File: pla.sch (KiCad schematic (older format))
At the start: 16 parts, among them U12 74LS02, U14 74LS139, U15 74LS175, U16 MOS_251641_PLA, U19 ATF16V8

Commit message: Enlarge drill holes to 0.9mm in order to make it possible to use ZIF sockets
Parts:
- U12: footprint Package_DIP:DIP-14_W7.62mm_Socket_LongPads -> LittleSixteen:DIP-14_W7.62mm_Socket_LongPads
- U14, U15: footprint Package_DIP:DIP-16_W7.62mm_Socket_LongPads -> LittleSixteen:DIP-16_W7.62mm_Socket_LongPads
- U16: footprint Package_DIP:DIP-28_W15.24mm_Socket_LongPads -> LittleSixteen:DIP-28_W15.24mm_Socket_LongPads
- U19: footprint Package_DIP:DIP-20_W7.62mm_Socket_LongPads -> LittleSixteen:DIP-20_W7.62mm_Socket_LongPads
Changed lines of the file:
@@
 F 0 "U14" H 9280 5531 50  0000 L CNN
 F 1 "74LS139" H 9280 5440 50  0000 L CNN
-F 2 "Package_DIP:DIP-16_W7.62mm_Socket_LongPads" H 9050 5485 50  0001 C CNN
+F 2 "LittleSixteen:DIP-16_W7.62mm_Socket_LongPads" H 9050 5485 50  0001 C CNN
 F 3 "http://www.ti.com/lit/gpn/sn74LS139" H 9050 5485 50  0001 C CNN
 	3    9050 5485
@@
 F 0 "U12" H 7495 5531 50  0000 L CNN
 F 1 "74LS02" H 7495 5440 50  0000 L CNN
-F 2 "Package_DIP:DIP-14_W7.62mm_Socket_LongPads" H 7265 5485 50  0001 C CNN
+F 2 "LittleSixteen:DIP-14_W7.62mm_Socket_LongPads" H 7265 5485 50  0001 C CNN
 F 3 "http://www.ti.com/lit/gpn/sn74ls02" H 7265 5485 50  0001 C CNN
 	5    7265 5485
@@
 F 0 "U19" H 3840 7075 50  0000 C CNN
 F 1 "ATF16V8" H 3840 6984 50  0000 C CNN
-F 2 "Package_DIP:DIP-20_W7.62mm_Socket_LongPads" H 3840 6260 50  0001 C CNN
+F 2 "LittleSixteen:DIP-20_W7.62mm_Socket_LongPads" H 3840 6260 50  0001 C CNN
 F 3 "DOCUMENTATION" H 3840 6260 50  0001 C CNN
 	1    3840 6260
@@
 F 0 "U16" H 2395 3200 50  0000 C CNN
 F 1 "MOS_251641_PLA" H 2395 3109 50  0000 C CNN
-F 2 "Package_DIP:DIP-28_W15.24mm_Socket_LongPads" H 2395 1985 50  0001 C CNN
+F 2 "LittleSixteen:DIP-28_W15.24mm_Socket_LongPads" H 2395 1985 50  0001 C CNN
 F 3 "DOCUMENTATION" H 2395 1985 50  0001 C CNN
 	1    2395 1985
@@
 F 0 "U16" H 8822 3576 50  0000 R CNN
 F 1 "MOS_251641_PLA" H 8822 3485 50  0000 R CNN
-F 2 "Package_DIP:DIP-28_W15.24mm_Socket_LongPads" H 9050 3530 50  0001 C CNN
+F 2 "LittleSixteen:DIP-28_W15.24mm_Socket_LongPads" H 9050 3530 50  0001 C CNN
 F 3 "DOCUMENTATION" H 9050 3530 50  0001 C CNN
 	2    9050 3530
@@
 F 0 "U12" H 8105 3075 50  0000 C CNN
 F 1 "74LS02" H 8105 2984 50  0000 C CNN
-F 2 "Package_DIP:DIP-14_W7.62mm_Socket_LongPads" H 8105 2750 50  0001 C CNN
+F 2 "LittleSixteen:DIP-14_W7.62mm_Socket_LongPads" H 8105 2750 50  0001 C CNN
 F 3 "http://www.ti.com/lit/gpn/sn74ls02" H 8105 2750 50  0001 C CNN
 	3    8105 2750
@@
 F 0 "U12" H 8105 2375 50  0000 C CNN
 F 1 "74LS02" H 8105 2284 50  0000 C CNN
-F 2 "Package_DIP:DIP-14_W7.62mm_Socket_LongPads" H 8105 2050 50  0001 C CNN
+F 2 "LittleSixteen:DIP-14_W7.62mm_Socket_LongPads" H 8105 2050 50  0001 C CNN
 F 3 "http://www.ti.com/lit/gpn/sn74ls02" H 8105 2050 50  0001 C CNN
 	2    8105 2050
@@
 F 0 "U14" H 9650 2517 50  0000 C CNN
 F 1 "74LS139" H 9650 2426 50  0000 C CNN
-F 2 "Package_DIP:DIP-16_W7.62mm_Socket_LongPads" H 9650 2150 50  0001 C CNN
+F 2 "LittleSixteen:DIP-16_W7.62mm_Socket_LongPads" H 9650 2150 50  0001 C CNN
 F 3 "http://www.ti.com/lit/gpn/sn74LS139" H 9650 2150 50  0001 C CNN
 	2    9650 2150
@@
 F 0 "U14" H 8115 1652 50  0000 C CNN
 F 1 "74LS139" H 8115 1561 50  0000 C CNN
-F 2 "Package_DIP:DIP-16_W7.62mm_Socket_LongPads" H 8115 1285 50  0001 C CNN
+F 2 "LittleSixteen:DIP-16_W7.62mm_Socket_LongPads" H 8115 1285 50  0001 C CNN
 F 3 "http://www.ti.com/lit/gpn/sn74LS139" H 8115 1285 50  0001 C CNN
 	1    8115 1285
@@
 F 0 "U12" H 4660 1668 50  0000 C CNN
 F 1 "74LS02" H 4660 1759 50  0000 C CNN
-F 2 "Package_DIP:DIP-14_W7.62mm_Socket_LongPads" H 4660 1985 50  0001 C CNN
+F 2 "LittleSixteen:DIP-14_W7.62mm_Socket_LongPads" H 4660 1985 50  0001 C CNN
 F 3 "http://www.ti.com/lit/gpn/sn74ls02" H 4660 1985 50  0001 C CNN
 	1    4660 1985
@@
 F 0 "U15" H 6380 2135 50  0000 C CNN
 F 1 "74LS175" H 6435 930 50  0000 C CNN
-F 2 "Package_DIP:DIP-16_W7.62mm_Socket_LongPads" H 6165 1585 50  0001 C CNN
+F 2 "LittleSixteen:DIP-16_W7.62mm_Socket_LongPads" H 6165 1585 50  0001 C CNN
 F 3 "http://www.ti.com/lit/gpn/sn74LS175" H 6165 1585 50  0001 C CNN
 	1    6165 1585

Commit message: Use clearer diode footprint
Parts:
- D80, D81, D82, D83, D84, D85: footprint Diode_THT:D_DO-35_SOD27_P5.08mm_Vertical_KathodeUp -> LittleSixteen:D_DO-35_SOD27_P5.08mm_Vertical_KathodeUp
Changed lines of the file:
@@
 F 0 "D80" H 2335 5455 50  0000 C CNN
 F 1 "1n4148" H 2325 5550 50  0000 C CNN
-F 2 "Diode_THT:D_DO-35_SOD27_P5.08mm_Vertical_KathodeUp" H 2225 5405 50  0001 C CNN
+F 2 "LittleSixteen:D_DO-35_SOD27_P5.08mm_Vertical_KathodeUp" H 2225 5405 50  0001 C CNN
 F 3 "~" H 2225 5405 50  0001 C CNN
 F 4 "Only mount if using PLA16V8" H 2225 5405 50  0001 C CNN "Notes"
@@
 F 0 "D81" H 2140 5265 50  0000 C CNN
 F 1 "1n4148" H 2025 5179 50  0001 C CNN
-F 2 "Diode_THT:D_DO-35_SOD27_P5.08mm_Vertical_KathodeUp" H 2025 5305 50  0001 C CNN
+F 2 "LittleSixteen:D_DO-35_SOD27_P5.08mm_Vertical_KathodeUp" H 2025 5305 50  0001 C CNN
 F 3 "~" H 2025 5305 50  0001 C CNN
 F 4 "Only mount if using PLA16V8" H 2025 5305 50  0001 C CNN "Notes"
@@
 F 0 "D82" H 2335 5165 50  0000 C CNN
 F 1 "1n4148" H 2225 5079 50  0001 C CNN
-F 2 "Diode_THT:D_DO-35_SOD27_P5.08mm_Vertical_KathodeUp" H 2225 5205 50  0001 C CNN
+F 2 "LittleSixteen:D_DO-35_SOD27_P5.08mm_Vertical_KathodeUp" H 2225 5205 50  0001 C CNN
 F 3 "~" H 2225 5205 50  0001 C CNN
 F 4 "Only mount if using PLA16V8" H 2225 5205 50  0001 C CNN "Notes"
@@
 F 0 "D83" H 2140 5065 50  0000 C CNN
 F 1 "1n4148" H 2025 4979 50  0001 C CNN
-F 2 "Diode_THT:D_DO-35_SOD27_P5.08mm_Vertical_KathodeUp" H 2025 5105 50  0001 C CNN
+F 2 "LittleSixteen:D_DO-35_SOD27_P5.08mm_Vertical_KathodeUp" H 2025 5105 50  0001 C CNN
 F 3 "~" H 2025 5105 50  0001 C CNN
 F 4 "Only mount if using PLA16V8" H 2025 5105 50  0001 C CNN "Notes"
@@
 F 0 "D84" H 2330 4970 50  0000 C CNN
 F 1 "1n4148" H 2225 4879 50  0001 C CNN
-F 2 "Diode_THT:D_DO-35_SOD27_P5.08mm_Vertical_KathodeUp" H 2225 5005 50  0001 C CNN
+F 2 "LittleSixteen:D_DO-35_SOD27_P5.08mm_Vertical_KathodeUp" H 2225 5005 50  0001 C CNN
 F 3 "~" H 2225 5005 50  0001 C CNN
 F 4 "Only mount if using PLA16V8" H 2225 5005 50  0001 C CNN "Notes"
@@
 F 0 "D85" H 2140 4865 50  0000 C CNN
 F 1 "1n4148" H 2025 4779 50  0001 C CNN
-F 2 "Diode_THT:D_DO-35_SOD27_P5.08mm_Vertical_KathodeUp" H 2025 4905 50  0001 C CNN
+F 2 "LittleSixteen:D_DO-35_SOD27_P5.08mm_Vertical_KathodeUp" H 2025 4905 50  0001 C CNN
 F 3 "~" H 2025 4905 50  0001 C CNN
 F 4 "Only mount if using PLA16V8" H 2025 4905 50  0001 C CNN "Notes"

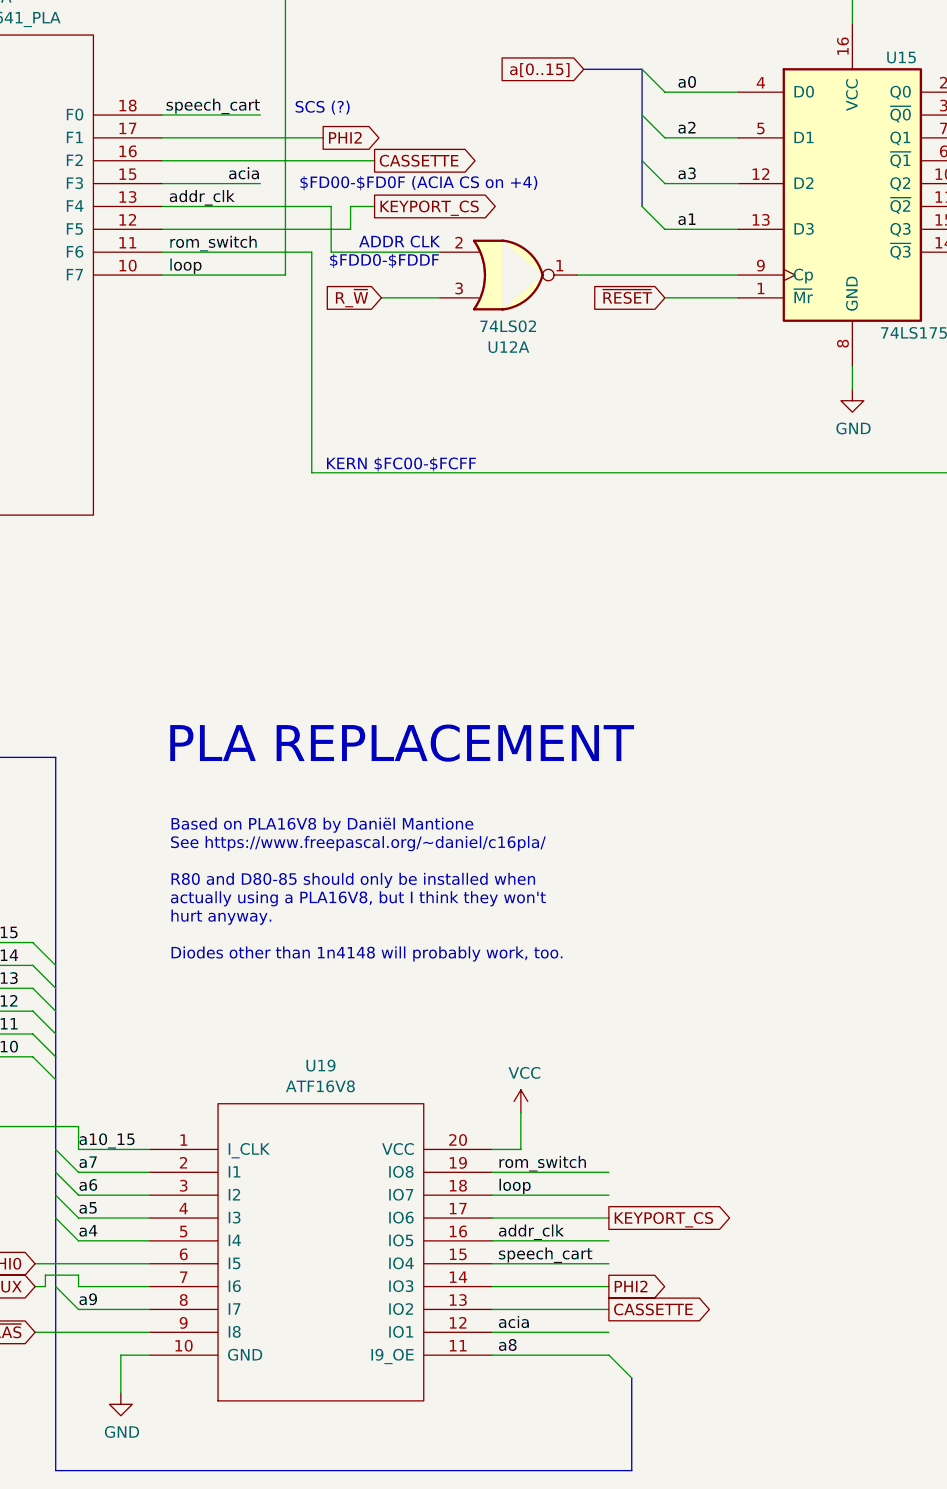
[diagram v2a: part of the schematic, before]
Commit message: Add userport schematics and enlarge board
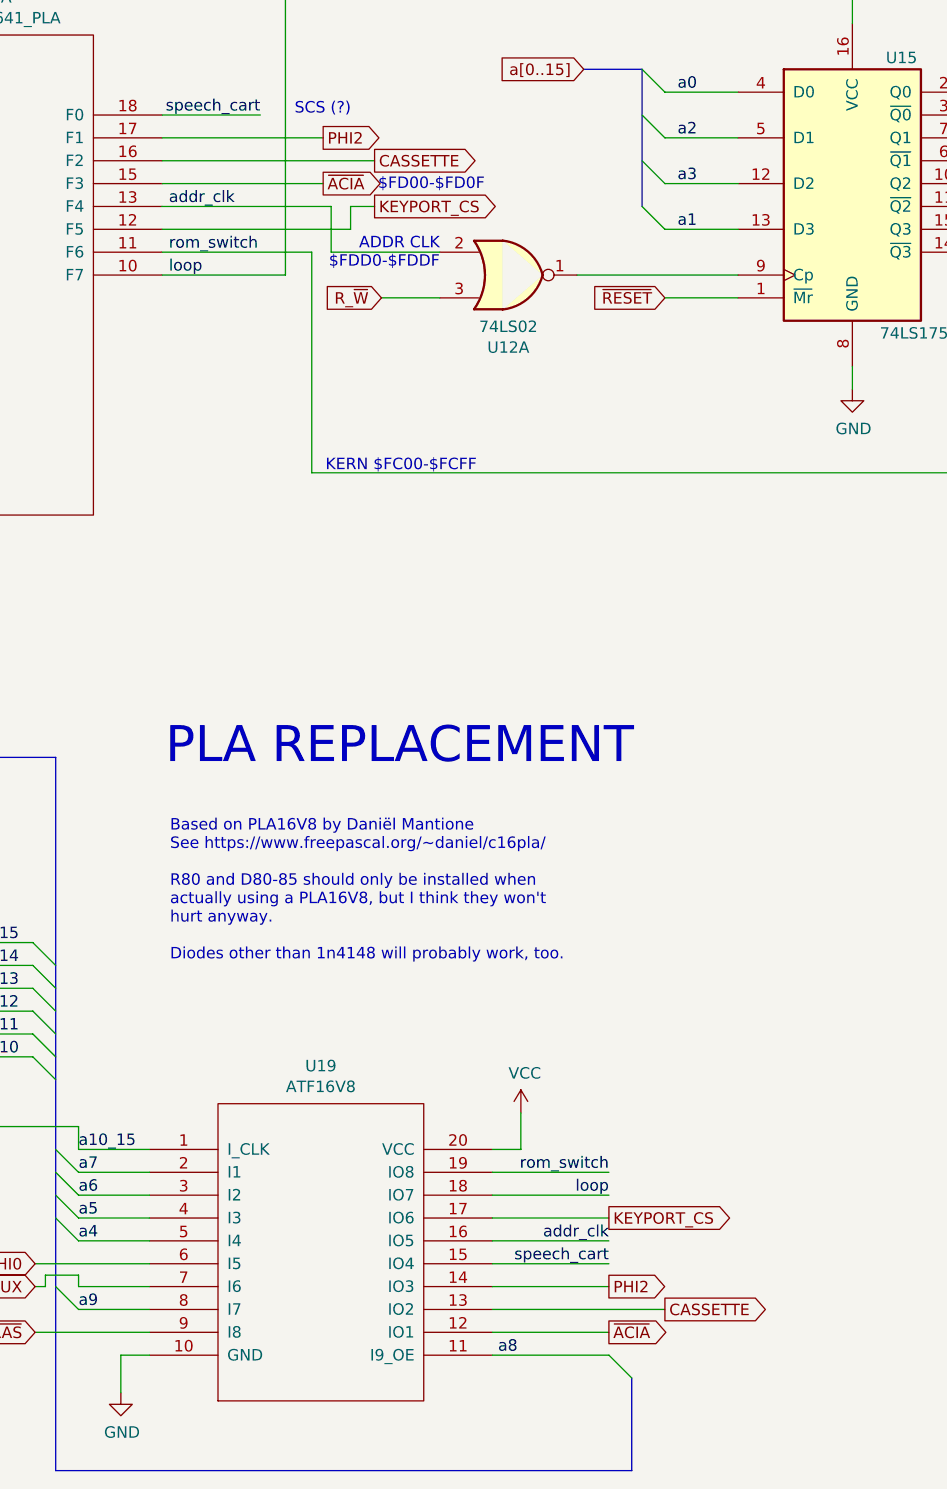
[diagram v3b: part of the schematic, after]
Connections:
- net labels added: ~ACIA
- net labels removed: acia
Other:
- note added: "$FD00-$FD0F"
- note removed: "$FD00-$FD0F (ACIA CS on +4)"
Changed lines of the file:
@@
 $Descr A4 11693 8268
 encoding utf-8
-Sheet 10 12
+Sheet 10 13
 Title "LittleSixteen"
 Date "2021-11-05"
@@
 	4590 6610 5100 6610
 Wire Wire Line
-	4590 6510 5100 6510
+	4590 6510 5345 6510
 Wire Wire Line
 	4590 6410 5100 6410
@@
 Wire Wire Line
 	4590 5910 5100 5910
-Text Label 4615 6610 0    50   ~ 0
-acia
-Text Label 4615 6210 0    50   ~ 0
+Text Label 5100 6210 2    50   ~ 0
 addr_clk
-Text Label 4615 5910 0    50   ~ 0
+Text Label 5100 5910 2    50   ~ 0
 rom_switch
-Text Label 4615 6010 0    50   ~ 0
+Text Label 5100 6010 2    50   ~ 0
 loop
-Text Label 4615 6310 0    50   ~ 0
+Text Label 5100 6310 2    50   ~ 0
 speech_cart
 Text Label 2780 5810 0    50   ~ 0
@@
 Text GLabel 5100 6410 2    50   Output ~ 0
 PHI2
-Text GLabel 5100 6510 2    50   Output ~ 0
+Text GLabel 5345 6510 2    50   Output ~ 0
 CASSETTE
 Text GLabel 5100 6110 2    50   Output ~ 0
@@
 Wire Wire Line
 	3145 1285 3575 1285
-Text Label 3575 1585 2    50   ~ 0
-acia
 Wire Wire Line
 	3800 1885 3800 2850
@@
 Wire Wire Line
 	3145 1385 3850 1385
-Text Notes 3745 1620 0    50   ~ 0
-$FD00-$FD0F (ACIA CS on +4)
+Text Notes 4090 1620 0    50   ~ 0
+$FD00-$FD0F
 Text Notes 3725 1290 0    50   ~ 0
 SCS (?)
@@
 $EndComp
 Wire Wire Line
-	3145 1585 3575 1585
+	3145 1585 3850 1585
 Text Label 3175 1685 0    50   ~ 0
 addr_clk
@@
 Wire Wire Line
 	10150 2150 10420 2150
+Text GLabel 3850 1585 2    50   Output ~ 0
+~ACIA
+Text GLabel 5100 6610 2    50   Output ~ 0
+~ACIA
 Wire Bus Line
 	5245 1085 5245 1685

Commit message: Place components on board
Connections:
- net a10_15 renamed A15_10_HIGH
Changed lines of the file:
@@
 Text GLabel 5100 6610 2    50   Output ~ 0
 ~ACIA
+Wire Wire Line
+	2780 5710 2780 5305
+Wire Wire Line
+	2780 5305 3205 5305
 Wire Bus Line
 	5245 1085 5245 1685
@@
 Wire Bus Line
 	2680 4095 2680 7215
+Connection ~ 2780 5710
+Text GLabel 3205 5305 2    50   Output ~ 0
+A15_10_HIGH
 $EndSCHEMATC

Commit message: Add 512kB RAM expansions, Hannes-style
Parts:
- removed unit 1 of U16
- removed U19: ATF16V8, LittleSixteen:DIP-20_W7.62mm_Socket_LongPads, symbol atf16v8:ATF16V8
- added U19: GAL16V8, Package_DIP:DIP-20_W7.62mm_Socket_LongPads, symbol Logic_Programmable:GAL16V8
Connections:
- net A15_10_HIGH: now also U19.1 (I1/CLK)
- net GND: now also U19.10 (GND)
- net KEYPORT_CS: now also U19.17 (I03)
- net MUX: now also U19.7 (I7)
- net PHI0: now also U19.6 (I6)
- net PHI2: now also U19.14 (IO6)
- net VCC: now also U19.20 (VCC)
- net a4: now also U19.5 (I5)
- net a5: now also U19.4 (I4)
- net a6: now also U19.3 (I3)
- net a7: now also U19.2 (I2)
- net a8: now also U19.11 (I10/~OE~)
- net a9: now also U19.8 (I8)
- net addr_clk: now also U19.16 (IO4)
- net loop: now also U19.18 (IO2)
- net rom_switch: now also U19.19 (IO1)
- net ~ACIA: now also U19.12 (IO8)
- net ~RAS: now also U19.9 (I9)
- new net ~JOY3: U19.15 (IO5)
- new net ~SID: U19.13 (IO7)
- no-connect marks 4 -> 5
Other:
- note added: "$FDD0-$FDDF"
- note added: "Modified version of PLA16V8 by Daniël Mantione\nSee https://www.freepascal.org/~~daniel/c16pla/\n- Does NOT produce userport ~CS~\n- Instead produces SID & 3rd joystick port ~CS~"
- note added: "PLA - 1 -"
- note removed: "ADDR CLK\n$FDD0-$FDDF"
- note removed: "Based on PLA16V8 by Daniël Mantione\nSee https://www.freepascal.org/~~daniel/c16pla/\n\nR80 and D80-85 should only be installed when\nactually using a PLA16V8, but I think they won't\nhurt anyway.\n\nDiodes other than 1n4148 will probably work, too."
- note removed: "PLA REPLACEMENT"
- note removed: "SCS (?)"
- note removed: "This enables function\nROM HIGH on the +4"
- note removed: "This enables function\nROM LOW on the +4"

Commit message: WIP
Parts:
- removed U16: MOS_251641_PLA, LittleSixteen:DIP-28_W15.24mm_Socket_LongPads, symbol MOS_251641_PLA:MOS_251641_PLA
- U19: footprint Package_DIP:DIP-20_W7.62mm_Socket_LongPads -> LittleSixteen:DIP-20_W7.62mm_Socket_LongPads
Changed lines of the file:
@@
 	1    0    0    -1
 $EndComp
-Wire Wire Line
-	9775 3675 9775 4175
-Wire Wire Line
-	9775 4175 9405 4175
-Wire Wire Line
-	9050 4175 9050 4030
-$Comp
-L power:GND #PWR0174
-U 1 1 5DEA08EA
-P 9405 4275
-F 0 "#PWR0174" H 9405 4025 50  0001 C CNN
-F 1 "GND" H 9410 4102 50  0000 C CNN
-F 2 "" H 9405 4275 50  0001 C CNN
-F 3 "" H 9405 4275 50  0001 C CNN
-	1    9405 4275
-	1    0    0    -1
-$EndComp
-Wire Wire Line
-	9405 4275 9405 4175
-Connection ~ 9405 4175
-Wire Wire Line
-	9405 4175 9050 4175
 $Comp
 L Device:C C91
@@
 	3800 2850 7050 2850
 Connection ~ 7050 2850
-Wire Wire Line
-	9405 2915 9775 2915
-Connection ~ 9405 2915
-Wire Wire Line
-	9405 2805 9405 2915
-$Comp
-L power:VCC #PWR0175
-U 1 1 5DEA08F7
-P 9405 2805
-F 0 "#PWR0175" H 9405 2655 50  0001 C CNN
-F 1 "VCC" H 9422 2978 50  0000 C CNN
-F 2 "" H 9405 2805 50  0001 C CNN
-F 3 "" H 9405 2805 50  0001 C CNN
-	1    9405 2805
-	1    0    0    -1
-$EndComp
-Wire Wire Line
-	9775 2915 9775 3375
-Wire Wire Line
-	9050 2915 9405 2915
-Wire Wire Line
-	9050 3030 9050 2915
-$Comp
-L Device:C C30
-U 1 1 5DEA08DA
-P 9775 3525
-F 0 "C30" H 9890 3571 50  0000 L CNN
-F 1 "100n" H 9890 3480 50  0000 L CNN
-F 2 "Capacitor_THT:C_Disc_D8.0mm_W2.5mm_P5.00mm" H 9813 3375 50  0001 C CNN
-F 3 "~" H 9775 3525 50  0001 C CNN
-	1    9775 3525
-	1    0    0    -1
-$EndComp
-$Comp
-L MOS_251641_PLA:MOS_251641_PLA U16
-U 2 1 5DE9421D
-P 9050 3530
-F 0 "U16" H 8822 3576 50  0000 R CNN
-F 1 "MOS_251641_PLA" H 8822 3485 50  0000 R CNN
-F 2 "LittleSixteen:DIP-28_W15.24mm_Socket_LongPads" H 9050 3530 50  0001 C CNN
-F 3 "DOCUMENTATION" H 9050 3530 50  0001 C CNN
-	2    9050 3530
-	1    0    0    -1
-$EndComp
 Text GLabel 10420 2350 2    50   Output ~ 0
 C2_HIGH
@@
 F 0 "U19" H 3855 6910 50  0000 C CNN
 F 1 "GAL16V8" H 3780 5705 50  0000 C CNN
-F 2 "Package_DIP:DIP-20_W7.62mm_Socket_LongPads" H 3590 6310 50  0001 C CNN
+F 2 "LittleSixteen:DIP-20_W7.62mm_Socket_LongPads" H 3590 6310 50  0001 C CNN
 F 3 "" H 3590 6310 50  0001 C CNN
 F 4 "556-AF16V8B15PU" H 3590 6310 50  0001 C CNN "MouserPN"
@@
 	2680 6610 2780 6710
 NoConn ~ 4600 5910
+Wire Wire Line
+	4275 7235 4275 7310
+Wire Wire Line
+	4275 6860 4275 6935
+$Comp
+L power:GND #PWR?
+U 1 1 64692107
+P 4275 7310
+AR Path="/5E4A465A/64692107" Ref="#PWR?"  Part="1"
+AR Path="/5EE7AAEB/64692107" Ref="#PWR0138"  Part="1"
+F 0 "#PWR0138" H 4275 7060 50  0001 C CNN
+F 1 "GND" H 4280 7137 50  0000 C CNN
+F 2 "" H 4275 7310 50  0001 C CNN
+F 3 "" H 4275 7310 50  0001 C CNN
+	1    4275 7310
+	1    0    0    -1
+$EndComp
+$Comp
+L power:VCC #PWR?
+U 1 1 64692111
+P 4275 6860
+AR Path="/5E4A465A/64692111" Ref="#PWR?"  Part="1"
+AR Path="/5EE7AAEB/64692111" Ref="#PWR0139"  Part="1"
+F 0 "#PWR0139" H 4275 6710 50  0001 C CNN
+F 1 "VCC" H 4292 7033 50  0000 C CNN
+F 2 "" H 4275 6860 50  0001 C CNN
+F 3 "" H 4275 6860 50  0001 C CNN
+	1    4275 6860
+	1    0    0    -1
+$EndComp
+$Comp
+L Device:C C?
+U 1 1 6469211B
+P 4275 7085
+AR Path="/5E4A465A/6469211B" Ref="C?"  Part="1"
+AR Path="/5EE7AAEB/6469211B" Ref="C30"  Part="1"
+F 0 "C30" H 4390 7131 50  0000 L CNN
+F 1 "100n" H 4390 7040 50  0000 L CNN
+F 2 "Capacitor_THT:C_Disc_D8.0mm_W2.5mm_P5.00mm" H 4313 6935 50  0001 C CNN
+F 3 "~" H 4275 7085 50  0001 C CNN
+	1    4275 7085
+	1    0    0    -1
+$EndComp
 Wire Bus Line
 	5245 1085 5245 1685
